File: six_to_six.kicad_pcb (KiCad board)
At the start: 2 copper layers, 545.4 x 309.1 mm, 468 parts, among them J1 Pads for coax, J10 Pads for coax, J11 Pads for coax, J12 Pads for coax, J13 BNC, J14 Pads for coax, J15 Pads for coax, J16 Pads for coax, J17 Pads for coax, J18 Relay control, J19 BNC, J2 Pads for coax, J20 Pads for coax, J21 Pads for coax, J22 Pads for coax, J23 BNC, J24 Pads for coax, J25 Pads for coax, J26 Pads for coax, J27 Pads for coax, J28 Relay control, J29 BNC, J3 BNC, J30 Pads for coax, J31 Pads for coax, J32 Pads for coax, J33 BNC, J34 Pads for coax, J35 Pads for coax, J36 Pads for coax, J37 Pads for coax, J38 Relay control, J39 BNC, J4 Pads for coax, J40 Pads for coax, J41 Pads for coax, J42 Pads for coax, J43 BNC, J44 Pads for coax, J45 Pads for coax, J46 Pads for coax, J47 Pads for coax, J48 Relay control, J49 BNC, J5 Pads for coax, J50 Pads for coax, J51 Pads for coax, J52 Pads for coax, J53 BNC, J54 Pads for coax, J55 Pads for coax, J56 Pads for coax, J57 Pads for coax, J58 Relay control, J59 BNC, J6 Pads for coax, J60 Pads for coax, J7 Pads for coax, J8 Relay control, J9 BNC, K1 RY-12W-K, K10 RY-12W-K, K11 RY-12W-K, K12 RY-12W-K, K13 RY-12W-K, K14 RY-12W-K, K15 RY-12W-K, K16 RY-12W-K, K17 RY-12W-K, K18 RY-12W-K, K19 RY-12W-K, K2 RY-12W-K, K20 RY-12W-K, K21 RY-12W-K, K22 RY-12W-K, K23 RY-12W-K, K24 RY-12W-K, K25 RY-12W-K, K26 RY-12W-K, K27 RY-12W-K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

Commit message: changed to 1 to 6
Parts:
- removed C12, C13, C17, C18, C19, C22, C23, C24, C28, C29, C30, C33, C34, C35, C39, C40, C41, C44, C45, C46, C50, C51, C52, C55, C56, C57, C61, C62, C63, C66: 100n, Capacitor_SMD:C_0603_1608Metric_Pad1.08x0.95mm_HandSolder
- removed C14, C25, C36, C47, C58: 100n, Capacitor_THT:C_Disc_D5.1mm_W3.2mm_P5.00mm
- removed C15, C16, C20, C21, C26, C27, C31, C32, C37, C38, C42, C43, C48, C49, C53, C54, C59, C60, C64, C65: 68p, Capacitor_THT:C_Disc_D5.1mm_W3.2mm_P5.00mm
- removed D11, D12, D17, D18, D19, D20, D21, D22, D27, D28, D29, D30, D31, D32, D37, D38, D39, D40, D41, D42, D47, D48, D49, D50, D51, D52, D57, D58, D59, D60: 1N4148W, Diode_SMD:D_SOD-123
- removed D13, D14, D15, D16, D23, D24, D25, D26, D33, D34, D35, D36, D43, D44, D45, D46, D53, D54, D55, D56: 1N4148, Diode_THT:D_DO-35_SOD27_P7.62mm_Horizontal
- removed F2, F3, F4, F5, F6: Polyfuse, Fuse:Fuse_BelFuse_0ZRE0005FF_L8.3mm_W3.8mm
- removed J10, J11, J12, J14, J15, J16, J20, J21, J22, J24, J25, J26, J30, J31, J32, J34, J35, J36, J40, J41, J42, J44, J45, J46, J50, J51, J52, J54, J55, J56, J60: Pads for coax, Connector_PinHeader_2.54mm:PinHeader_2x02_P2.54mm_Vertical
- removed J13, J19, J23, J29, J33, J39, J43, J49, J53, J59, J9: BNC, Components:BNC_vertical
- removed J17, J27, J37, J47, J57: Pads for coax, Connector_PinHeader_2.54mm:PinHeader_1x02_P2.54mm_Vertical
- removed J18, J28, J38, J48, J58: Relay control, Connector_PinHeader_2.54mm:PinHeader_2x04_P2.54mm_Vertical
- removed JP10, JP11, JP12, JP3, JP4, JP5, JP6, JP7, JP8, JP9: 50/75 ohm, Connector_PinHeader_2.54mm:PinHeader_1x03_P2.54mm_Vertical
- removed K10, K11, K12, K13, K14, K15, K16, K17, K18, K19, K20, K21, K22, K23, K24, K25, K26, K27, K28, K29, K30, K31, K32, K33, K34, K35, K36, K7, K8, K9: RY-12W-K, Components:RELAY_RY-12W-K
- removed NE2, NE3, NE4, NE5, NE6: Lamp_Neon, LED_THT:LED_D5.0mm_Clear
- removed Q10, Q11, Q12, Q13, Q14, Q15, Q16, Q17, Q18, Q19, Q20, Q21, Q22, Q23, Q24, Q25, Q26, Q27, Q28, Q29, Q30, Q31, Q32, Q33, Q34, Q35, Q36, Q7, Q8, Q9: MMBT3904, Package_TO_SOT_SMD:SOT-23
- removed R100, R101, R102, R24, R25, R26, R43, R44, R45, R62, R63, R64, R81, R82, R83: 68E, Resistor_THT:R_Axial_DIN0411_L9.9mm_D3.6mm_P12.70mm_Horizontal
- removed R103, R27, R46, R65, R84: 18E, Resistor_THT:R_Axial_DIN0411_L9.9mm_D3.6mm_P12.70mm_Horizontal
- removed R104, R111, R112, R28, R35, R36, R47, R54, R55, R66, R73, R74, R85, R92, R93: 100E, Resistor_THT:R_Axial_DIN0411_L9.9mm_D3.6mm_P12.70mm_Horizontal
- removed R105, R107, R109, R113, R20, R22, R29, R31, R33, R37, R39, R41, R48, R50, R52, R56, R58, R60, R67, R69, R71, R75, R77, R79, R86, R88, R90, R94, R96, R98: 3k3, Resistor_SMD:R_0603_1608Metric_Pad0.98x0.95mm_HandSolder
- removed R106, R108, R110, R114, R21, R23, R30, R32, R34, R38, R40, R42, R49, R51, R53, R57, R59, R61, R68, R70, R72, R76, R78, R80, R87, R89, R91, R95, R97, R99: 50E, Resistor_SMD:R_1210_3225Metric_Pad1.30x2.65mm_HandSolder
- removed TR13, TR25, TR37, TR49, TR61: BN-73-6802, Components:BN-73-6802-balun
- removed TR14, TR26, TR38, TR50, TR62: BN-73-transformer, Components:BN-73-202-1-1
- removed TR15, TR16, TR27, TR28, TR39, TR40, TR51, TR52, TR63, TR64: BN-73-202, Components:BN-73-202-2-0
- removed TR17, TR18, TR29, TR30, TR41, TR42, TR53, TR54, TR65, TR66: BN-73-6802, Components:BN-73-6802-2-0
- removed TR19, TR21, TR23, TR31, TR33, TR35, TR43, TR45, TR47, TR55, TR57, TR59, TR67, TR69, TR71: BN-73-6802, Components:BN-73-6802-3-0
- removed TR20, TR22, TR24, TR32, TR34, TR36, TR44, TR46, TR48, TR56, TR58, TR60, TR68, TR70, TR72: BN-73-6802, Components:BN-73-202-2-0
- C1, C2, C6, D1, D10, D2, D7, D8, D9, Q1, Q2, Q3, Q4, Q5, Q6, R10, R12, R2, R4: moved to B.Cu
- C10, C4, C5: value 68p -> 100n; footprint Capacitor_THT:C_Disc_D5.1mm_W3.2mm_P5.00mm -> Capacitor_SMD:C_0603_1608Metric_Pad1.08x0.95mm_HandSolder; moved to B.Cu
- C11, C7, C8: value 100n -> 68p; footprint Capacitor_SMD:C_0603_1608Metric_Pad1.08x0.95mm_HandSolder -> Capacitor_SMD:C_0805_2012Metric_Pad1.18x1.45mm_HandSolder; moved to B.Cu
- C3: footprint Capacitor_THT:C_Disc_D5.1mm_W3.2mm_P5.00mm -> Capacitor_SMD:C_0603_1608Metric_Pad1.08x0.95mm_HandSolder; moved to B.Cu
- C9: footprint Capacitor_THT:C_Disc_D5.1mm_W3.2mm_P5.00mm -> Capacitor_SMD:C_0805_2012Metric_Pad1.18x1.45mm_HandSolder; moved to B.Cu
- D3, D4, D5, D6: value 1N4148 -> 1N4148W; footprint Diode_THT:D_DO-35_SOD27_P7.62mm_Horizontal -> Diode_SMD:D_SOD-123; moved to B.Cu
- J1, J2, J4, J5, J6: value Pads for coax -> pads for coax; footprint Connector_PinHeader_2.54mm:PinHeader_2x02_P2.54mm_Vertical -> Components:Coax_pad
- J3: value BNC -> pads for coax; footprint Components:BNC_vertical -> Components:Coax_pad
- J7: value Pads for coax -> BNC; footprint Connector_PinHeader_2.54mm:PinHeader_1x02_P2.54mm_Vertical -> Components:BNC_vertical
- R1, R3: value 3k3 -> 50E; footprint Resistor_SMD:R_0603_1608Metric_Pad0.98x0.95mm_HandSolder -> Resistor_SMD:R_1210_3225Metric_Pad1.30x2.65mm_HandSolder; moved to B.Cu
- R11: value 50E -> 3k3; footprint Resistor_SMD:R_1210_3225Metric_Pad1.30x2.65mm_HandSolder -> Resistor_SMD:R_0603_1608Metric_Pad0.98x0.95mm_HandSolder; moved to B.Cu
- R13, R15: value 50E -> 100E; footprint Resistor_SMD:R_1210_3225Metric_Pad1.30x2.65mm_HandSolder -> Resistor_SMD:R_1206_3216Metric_Pad1.30x1.75mm_HandSolder; moved to B.Cu
- R14: value 3k3 -> 100E; footprint Resistor_SMD:R_0603_1608Metric_Pad0.98x0.95mm_HandSolder -> Resistor_SMD:R_1206_3216Metric_Pad1.30x1.75mm_HandSolder; moved to B.Cu
- R16, R17: value 100E -> 68E; footprint Resistor_THT:R_Axial_DIN0411_L9.9mm_D3.6mm_P12.70mm_Horizontal -> Resistor_SMD:R_1206_3216Metric_Pad1.30x1.75mm_HandSolder; moved to B.Cu
- R18: value 3k3 -> 68E; footprint Resistor_SMD:R_0603_1608Metric_Pad0.98x0.95mm_HandSolder -> Resistor_SMD:R_1206_3216Metric_Pad1.30x1.75mm_HandSolder; moved to B.Cu
- R19: value 50E -> 18E; footprint Resistor_SMD:R_1210_3225Metric_Pad1.30x2.65mm_HandSolder -> Resistor_SMD:R_1206_3216Metric_Pad1.30x1.75mm_HandSolder; moved to B.Cu
- R5, R6: value 68E -> 50E; footprint Resistor_THT:R_Axial_DIN0411_L9.9mm_D3.6mm_P12.70mm_Horizontal -> Resistor_SMD:R_1210_3225Metric_Pad1.30x2.65mm_HandSolder; moved to B.Cu
- R7: value 68E -> 3k3; footprint Resistor_THT:R_Axial_DIN0411_L9.9mm_D3.6mm_P12.70mm_Horizontal -> Resistor_SMD:R_0603_1608Metric_Pad0.98x0.95mm_HandSolder; moved to B.Cu
- R8: value 18E -> 3k3; footprint Resistor_THT:R_Axial_DIN0411_L9.9mm_D3.6mm_P12.70mm_Horizontal -> Resistor_SMD:R_0603_1608Metric_Pad0.98x0.95mm_HandSolder; moved to B.Cu
- R9: value 100E -> 3k3; footprint Resistor_THT:R_Axial_DIN0411_L9.9mm_D3.6mm_P12.70mm_Horizontal -> Resistor_SMD:R_0603_1608Metric_Pad0.98x0.95mm_HandSolder; moved to B.Cu
- TR1: footprint Components:BN-73-6802-balun -> Components:BN-73-6802-3-0
- TR10: footprint Components:BN-73-202-2-0 -> Components:BN-73-6802-2-0
- TR11: footprint Components:BN-73-6802-3-0 -> Components:BN-73-6802-balun
- TR12: value BN-73-6802 -> BN-73-transformer; footprint Components:BN-73-202-2-0 -> Components:BN-73-202-1-1
- TR2: value BN-73-transformer -> BN-73-6802; footprint Components:BN-73-202-1-1 -> Components:BN-73-202-2-0
- TR3: value BN-73-202 -> BN-73-6802; footprint Components:BN-73-202-2-0 -> Components:BN-73-6802-3-0
- TR4: value BN-73-202 -> BN-73-6802
- TR5: footprint Components:BN-73-6802-2-0 -> Components:BN-73-6802-3-0
- TR6: footprint Components:BN-73-6802-2-0 -> Components:BN-73-202-2-0
- TR7: value BN-73-6802 -> BN-73-202; footprint Components:BN-73-6802-3-0 -> Components:BN-73-202-2-0
- TR8: value BN-73-6802 -> BN-73-202
- TR9: footprint Components:BN-73-6802-3-0 -> Components:BN-73-6802-2-0
- moved C5 445.8 mm to (718.8, 217.2), turned to 180 degrees
- moved R9 441.8 mm to (722.6, 195.6), turned to 90 degrees
- moved TR8 408.5 mm to (622.3, 189.2)
- moved TR7 382.7 mm to (622.3, 207.0)
- moved Q3 326.4 mm to (718.8, 195.6), turned to 180 degrees
- moved K3 320.3 mm to (723.9, 195.6)
- moved D7 309.6 mm to (596.9, 180.3), turned to 180 degrees
- moved R11 307.5 mm to (722.6, 220.7), turned to 90 degrees
- moved J4 307.0 mm to (745.5, 211.1), turned to 180 degrees
- moved R10 296.0 mm to (722.6, 208.3), turned to 90 degrees
- moved C9 293.0 mm to (673.1, 228.6), turned to 180 degrees
- moved C6 292.4 mm to (718.8, 229.9), turned to 180 degrees
- moved TR9 288.8 mm to (613.4, 171.4)
- moved D9 267.6 mm to (603.6, 185.4), turned to 180 degrees
- moved TR10 265.1 mm to (613.4, 224.8)
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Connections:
- C1 pad 1: Net-(C1-Pad1) -> Net-(Q1-Pad1)
- C10 pad 2: GND -> Net-(C10-Pad2)
- C11 pad 1: Net-(C11-Pad1) -> Net-(TR7-Pad2)
- C2 pad 1: Net-(C2-Pad1) -> Net-(Q2-Pad1)
- C3 pad 1: Net-(C3-Pad1) -> Net-(Q3-Pad1)
- C3 pad 2: Net-(C3-Pad2) -> GND
- C4 pad 1: Net-(C4-Pad1) -> Net-(Q4-Pad1)
- C5 pad 1: Net-(C5-Pad1) -> Net-(Q5-Pad1)
- C6 pad 1: Net-(C6-Pad1) -> Net-(Q6-Pad1)
- C7 pad 1: Net-(C7-Pad1) -> Net-(TR1-Pad2)
- C8 pad 1: Net-(C8-Pad1) -> Net-(TR3-Pad2)
- C9 pad 1: Net-(C9-Pad1) -> Net-(TR5-Pad2)
- D10 pad 1: +12V -> Net-(D8-Pad2)
- D10 pad 2: Net-(D10-Pad2) -> Net-(D7-Pad1)
- D3 pad 1: Net-(D3-Pad1) -> +12V
- D3 pad 2: Net-(D3-Pad2) -> Net-(K3-Pad16)
- D4 pad 1: Net-(D3-Pad2) -> +12V
- D4 pad 2: GND -> Net-(K4-Pad16)
- D5 pad 1: Net-(D5-Pad1) -> +12V
- D5 pad 2: Net-(D3-Pad1) -> Net-(K5-Pad16)
- D6 pad 1: GND -> +12V
- D6 pad 2: Net-(D5-Pad1) -> Net-(K6-Pad16)
- D7 pad 1: +12V -> Net-(D7-Pad1)
- D7 pad 2: Net-(D7-Pad2) -> GND
- D8 pad 1: +12V -> Net-(D8-Pad1)
- D9 pad 1: +12V -> GND
- D9 pad 2: Net-(D9-Pad2) -> Net-(D8-Pad1)
- F1 pad 1: Net-(C3-Pad2) -> Net-(C10-Pad2)
- F1 pad 2: Net-(D3-Pad1) -> Net-(D8-Pad2)
- J1 pad 1: Net-(J1-Pad1) -> GND
- J1 pad 2: Net-(J1-Pad1) -> Net-(K1-Pad9)
- J2 pad 1: Net-(J2-Pad1) -> GND
- J2 pad 2: Net-(J2-Pad1) -> Net-(K2-Pad9)
- J3 pad 1: Net-(J3-Pad1) -> GND
- J3 pad 2: Net-(J3-Pad2) -> Net-(K3-Pad9)
- J4 pad 1: Net-(J4-Pad1) -> GND
- J4 pad 2: Net-(J4-Pad1) -> Net-(K4-Pad9)
- J5 pad 1: Net-(J5-Pad1) -> GND
- J5 pad 2: Net-(J5-Pad1) -> Net-(J5-Pad2)
- J6 pad 1: Net-(J6-Pad1) -> GND
- J6 pad 2: Net-(J6-Pad1) -> Net-(K6-Pad9)
- J7 pad 1: GND -> Net-(J7-Pad1)
- JP1 pad 2: Net-(D3-Pad1) -> Net-(D8-Pad2)
- K1 pad 13: /One to Six splitter/2-Way Splitter1/RF-out-2 -> /One to Six splitter/2-Way Splitter1/RF-out-1
- K1 pad 9: Net-(J1-Pad1) -> Net-(K1-Pad9)
- K2 pad 13: /One to Six splitter/2-Way Splitter3/RF-out-2 -> /One to Six splitter/2-Way Splitter1/RF-out-2
- K2 pad 9: Net-(J2-Pad1) -> Net-(K2-Pad9)
- K3 pad 13: /One to Six splitter/2-Way Splitter3/RF-out-1 -> /One to Six splitter/2-Way Splitter2/RF-out-1
- K3 pad 16: Net-(D7-Pad2) -> Net-(K3-Pad16)
- K3 pad 9: Net-(J4-Pad1) -> Net-(K3-Pad9)
- K4 pad 16: Net-(D8-Pad2) -> Net-(K4-Pad16)
- K4 pad 9: Net-(J5-Pad1) -> Net-(K4-Pad9)
- K5 pad 13: /One to Six splitter/2-Way Splitter2/RF-out-1 -> /One to Six splitter/2-Way Splitter3/RF-out-1
- K5 pad 16: Net-(D9-Pad2) -> Net-(K5-Pad16)
- K5 pad 9: Net-(J6-Pad1) -> Net-(J5-Pad2)
- K6 pad 13: /One to Six splitter/2-Way Splitter1/RF-out-1 -> /One to Six splitter/2-Way Splitter3/RF-out-2
- K6 pad 16: Net-(D10-Pad2) -> Net-(K6-Pad16)
- K6 pad 9: Net-(J10-Pad1) -> Net-(K6-Pad9)
- NE1 pad 1: Net-(J3-Pad2) -> Net-(J7-Pad2)
- NE1 pad 2: Net-(J3-Pad1) -> Net-(J7-Pad1)
- Q1 pad 1: Net-(C1-Pad1) -> Net-(Q1-Pad1)
- Q2 pad 1: Net-(C2-Pad1) -> Net-(Q2-Pad1)
- Q3 pad 1: Net-(C6-Pad1) -> Net-(Q3-Pad1)
- Q3 pad 3: Net-(D7-Pad2) -> Net-(K3-Pad16)
- Q4 pad 1: Net-(C7-Pad1) -> Net-(Q4-Pad1)
- Q4 pad 3: Net-(D8-Pad2) -> Net-(K4-Pad16)
- Q5 pad 1: Net-(C8-Pad1) -> Net-(Q5-Pad1)
- Q5 pad 3: Net-(D9-Pad2) -> Net-(K5-Pad16)
- Q6 pad 1: Net-(C11-Pad1) -> Net-(Q6-Pad1)
- Q6 pad 3: Net-(D10-Pad2) -> Net-(K6-Pad16)
- R1 pad 1: /One to Six splitter/Connectors/Relay-2 -> Net-(K1-Pad11)
- R1 pad 2: Net-(C1-Pad1) -> GND
- R10 pad 1: /One to Six splitter/Connectors/Relay-3 -> /One to Six splitter/Connectors/Relay-4
- R10 pad 2: Net-(C6-Pad1) -> Net-(Q4-Pad1)
- R11 pad 1: Net-(K3-Pad11) -> /One to Six splitter/Connectors/Relay-5
- R11 pad 2: GND -> Net-(Q5-Pad1)
- R12 pad 2: Net-(C7-Pad1) -> Net-(Q6-Pad1)
- R13 pad 1: Net-(K4-Pad11) -> /One to Six splitter/2-Way Splitter1/RF-out-1
- R13 pad 2: GND -> /One to Six splitter/2-Way Splitter1/RF-out-2
- R14 pad 1: /One to Six splitter/Connectors/Relay-5 -> /One to Six splitter/2-Way Splitter2/RF-out-1
- R14 pad 2: Net-(C8-Pad1) -> /One to Six splitter/2-Way Splitter2/RF-out-2
- R15 pad 1: Net-(K5-Pad11) -> /One to Six splitter/2-Way Splitter3/RF-out-1
- R15 pad 2: GND -> /One to Six splitter/2-Way Splitter3/RF-out-2
- R16 pad 1: /One to Six splitter/2-Way Splitter2/RF-out-1 -> Net-(TR8-Pad1)
- R16 pad 2: /One to Six splitter/2-Way Splitter2/RF-out-2 -> Net-(TR8-Pad4)
- R17 pad 1: /One to Six splitter/2-Way Splitter1/RF-out-1 -> /One to Six splitter/2-Way Splitter1/RF-in
- R17 pad 2: /One to Six splitter/2-Way Splitter1/RF-out-2 -> Net-(TR9-Pad4)
- R18 pad 1: /One to Six splitter/Connectors/Relay-1 -> Net-(TR9-Pad4)
- R18 pad 2: Net-(C11-Pad1) -> /One to Six splitter/2-Way Splitter3/RF-in
- R19 pad 1: Net-(K6-Pad11) -> /One to Six splitter/2-Way Splitter2/RF-in
- R19 pad 2: GND -> Net-(TR9-Pad4)
- R2 pad 1: Net-(K1-Pad11) -> Net-(K2-Pad11)
- R3 pad 1: /One to Six splitter/Connectors/Relay-4 -> Net-(K3-Pad11)
- R3 pad 2: Net-(C2-Pad1) -> GND
- R4 pad 1: Net-(K2-Pad11) -> Net-(K4-Pad11)
- R5 pad 1: Net-(R5-Pad1) -> Net-(K5-Pad11)
- R5 pad 2: Net-(R5-Pad2) -> GND
- R6 pad 1: /One to Six splitter/2-Way Splitter1/RF-in -> Net-(K6-Pad11)
- R6 pad 2: Net-(R6-Pad2) -> GND
- R7 pad 1: Net-(R6-Pad2) -> /One to Six splitter/Connectors/Relay-1
- R7 pad 2: /One to Six splitter/2-Way Splitter2/RF-in -> Net-(Q1-Pad1)
- R8 pad 1: /One to Six splitter/2-Way Splitter3/RF-in -> /One to Six splitter/Connectors/Relay-2
- R8 pad 2: Net-(R6-Pad2) -> Net-(Q2-Pad1)
- R9 pad 1: /One to Six splitter/2-Way Splitter3/RF-out-1 -> /One to Six splitter/Connectors/Relay-3
- R9 pad 2: /One to Six splitter/2-Way Splitter3/RF-out-2 -> Net-(Q3-Pad1)
- TR1 pad 1: Net-(J3-Pad1) -> /One to Six splitter/2-Way Splitter1/RF-in
- TR1 pad 2: Net-(C3-Pad1) -> Net-(TR1-Pad2)
- TR1 pad 3: Net-(J3-Pad2) -> Net-(TR1-Pad2)
- TR1 pad 4: GND -> Net-(TR1-Pad4)
- TR10 pad 1: /One to Six splitter/2-Way Splitter2/RF-out-1 -> Net-(TR9-Pad4)
- TR10 pad 2: Net-(C9-Pad1) -> Net-(TR8-Pad4)
- TR10 pad 3: Net-(C9-Pad1) -> Net-(TR8-Pad4)
- TR10 pad 4: /One to Six splitter/2-Way Splitter2/RF-out-2 -> /One to Six splitter/2-Way Splitter3/RF-in
- TR11 pad 1: /One to Six splitter/2-Way Splitter1/RF-in -> Net-(J7-Pad1)
- TR11 pad 3: Net-(C10-Pad1) -> Net-(J7-Pad2)
- TR11 pad 4: Net-(TR11-Pad4) -> GND
- TR12 pad 1: /One to Six splitter/2-Way Splitter1/RF-out-1 -> Net-(JP1-Pad1)
- TR12 pad 2: Net-(C10-Pad1) -> GND
- TR12 pad 3: Net-(C10-Pad1) -> Net-(JP2-Pad1)
- TR12 pad 4: /One to Six splitter/2-Way Splitter1/RF-out-2 -> GND
- TR2 pad 1: Net-(JP1-Pad1) -> /One to Six splitter/2-Way Splitter1/RF-out-1
- TR2 pad 2: GND -> Net-(TR1-Pad2)
- TR2 pad 3: Net-(JP2-Pad1) -> Net-(TR1-Pad2)
- TR2 pad 4: GND -> /One to Six splitter/2-Way Splitter1/RF-out-2
- TR3 pad 1: /One to Six splitter/3-Way Splitter/RF-in -> /One to Six splitter/2-Way Splitter2/RF-in
- TR3 pad 2: Net-(C4-Pad1) -> Net-(TR3-Pad2)
- TR3 pad 3: Net-(C4-Pad1) -> Net-(TR3-Pad2)
- TR3 pad 4: GND -> Net-(TR3-Pad4)
- TR4 pad 1: Net-(R5-Pad1) -> /One to Six splitter/2-Way Splitter2/RF-out-1
- TR4 pad 2: Net-(C4-Pad1) -> Net-(TR3-Pad2)
- TR4 pad 3: Net-(C4-Pad1) -> Net-(TR3-Pad2)
- TR4 pad 4: Net-(R5-Pad2) -> /One to Six splitter/2-Way Splitter2/RF-out-2
- TR5 pad 1: /One to Six splitter/2-Way Splitter1/RF-in -> /One to Six splitter/2-Way Splitter3/RF-in
- TR5 pad 2: Net-(R5-Pad1) -> Net-(TR5-Pad2)
- TR5 pad 3: Net-(R5-Pad1) -> Net-(TR5-Pad2)
- TR5 pad 4: Net-(R6-Pad2) -> Net-(TR5-Pad4)
- TR6 pad 1: Net-(R6-Pad2) -> /One to Six splitter/2-Way Splitter3/RF-out-1
- TR6 pad 2: Net-(R5-Pad2) -> Net-(TR5-Pad2)
- TR6 pad 3: Net-(R5-Pad2) -> Net-(TR5-Pad2)
- TR6 pad 4: /One to Six splitter/2-Way Splitter2/RF-in -> /One to Six splitter/2-Way Splitter3/RF-out-2
- TR7 pad 1: /One to Six splitter/2-Way Splitter3/RF-in -> /One to Six splitter/3-Way Splitter/RF-in
- TR7 pad 2: Net-(C5-Pad1) -> Net-(TR7-Pad2)
- TR7 pad 3: Net-(C5-Pad1) -> Net-(TR7-Pad2)
- TR7 pad 4: Net-(TR7-Pad4) -> GND
- TR8 pad 1: /One to Six splitter/2-Way Splitter3/RF-out-1 -> Net-(TR8-Pad1)
- TR8 pad 2: Net-(C5-Pad1) -> Net-(TR7-Pad2)
- TR8 pad 3: Net-(C5-Pad1) -> Net-(TR7-Pad2)
- TR8 pad 4: /One to Six splitter/2-Way Splitter3/RF-out-2 -> Net-(TR8-Pad4)
- TR9 pad 1: /One to Six splitter/2-Way Splitter2/RF-in -> /One to Six splitter/2-Way Splitter1/RF-in
- TR9 pad 2: Net-(C9-Pad1) -> Net-(TR8-Pad1)
- TR9 pad 3: Net-(C9-Pad1) -> Net-(TR8-Pad1)
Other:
- board size 545.4 x 309.1 mm -> 190.5 x 88.9 mm

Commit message: pcb routed and made gerbers
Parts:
- removed J4, J5, J6: pads for coax, Components:Coax_pad
- removed J8: Relay control, Connector_PinHeader_2.54mm:PinHeader_2x04_P2.54mm_Vertical
- removed JP1, JP2: 50/75 ohm, Connector_PinHeader_2.54mm:PinHeader_1x03_P2.54mm_Vertical
- removed TR12: BN-73-transformer, Components:BN-73-202-1-1
- added H1: M3, MountingHole:MountingHole_3.2mm_M3_DIN965_Pad, F.Cu at (646.4, 232.4)
- added H2: M3, MountingHole:MountingHole_3.2mm_M3_DIN965_Pad, F.Cu at (738.5, 232.4)
- added H3: M3, MountingHole:MountingHole_3.2mm_M3_DIN965_Pad, F.Cu at (738.5, 163.8)
- J1: value pads for coax -> RF Conn; footprint Components:Coax_pad -> Components:PinHeader_2x06_P2.54mm_Horizontal
- J2: value pads for coax -> limiter; footprint Components:Coax_pad -> Connector_PinHeader_2.54mm:PinHeader_1x02_P2.54mm_Vertical
- J3: value pads for coax -> Relay control; footprint Components:Coax_pad -> Connector_PinHeader_2.54mm:PinHeader_2x04_P2.54mm_Vertical
- J7: footprint Components:BNC_vertical -> Components:BNC_horizontal
- moved J2 102.7 mm to (645.4, 162.7), turned to 0 degrees
- moved C10 73.0 mm to (652.0, 163.4), turned to 90 degrees
- moved TR11 70.6 mm to (647.1, 202.2)
- moved J7 70.0 mm to (649.0, 219.1), turned to 90 degrees
- moved NE1 59.2 mm to (650.7, 208.0)
- moved F1 58.3 mm to (654.6, 164.3), turned to 180 degrees
- moved D10 55.6 mm to (651.8, 176.4), turned to -90 degrees
- moved TR10 54.9 mm to (659.1, 194.3)
- moved D7 54.9 mm to (651.8, 182.4), turned to -90 degrees
- moved TR9 46.4 mm to (659.1, 163.8)
- moved TR7 46.2 mm to (659.1, 179.1)
- moved R18 45.9 mm to (664.2, 198.1), turned to -90 degrees
- moved J3 44.3 mm to (719.5, 234.3), turned to 90 degrees
- moved D9 42.9 mm to (646.4, 182.4), turned to 90 degrees
- moved D8 42.1 mm to (646.4, 176.4), turned to 90 degrees
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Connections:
- D10 pad 1: Net-(D8-Pad2) -> Net-(D10-Pad1)
- D8 pad 2: Net-(D8-Pad2) -> Net-(D10-Pad1)
- F1 pad 2: Net-(D8-Pad2) -> /One to Six splitter/3-Way Splitter/RF-in
- J1 pad 1: GND -> /One to Six splitter/Connectors/RF-1
- J1 pad 2: Net-(K1-Pad9) -> GND
- J2 pad 1: GND -> /One to Six splitter/3-Way Splitter/RF-in
- J2 pad 2: Net-(K2-Pad9) -> Net-(D10-Pad1)
- J3 pad 2: Net-(K3-Pad9) -> +12V
- K1 pad 9: Net-(K1-Pad9) -> /One to Six splitter/Connectors/RF-1
- K2 pad 9: Net-(K2-Pad9) -> /One to Six splitter/Connectors/RF-2
- K3 pad 9: Net-(K3-Pad9) -> /One to Six splitter/Connectors/RF-3
- K4 pad 9: Net-(K4-Pad9) -> /One to Six splitter/Connectors/RF-4
- K5 pad 9: Net-(J5-Pad2) -> /One to Six splitter/Connectors/RF-5
- K6 pad 9: Net-(K6-Pad9) -> /One to Six splitter/Connectors/RF-6
- TR11 pad 1: Net-(J7-Pad1) -> Net-(J7-Pad2)
- TR11 pad 2: Net-(C10-Pad1) -> GND
- TR11 pad 3: Net-(J7-Pad2) -> Net-(J7-Pad1)
- TR11 pad 4: GND -> Net-(C10-Pad1)
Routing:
- net GND: track 0.00 -> 469.5 mm, vias 0 -> 12
- net /One to Six splitter/Connectors/Relay-1: track 0.00 -> 83.8 mm
- net +12V: track 0.00 -> 71.3 mm
- net /One to Six splitter/Connectors/Relay-2: track 0.00 -> 63.1 mm
- net Net-(R16-Pad1): track 0.00 -> 58.9 mm
- net Net-(C9-Pad1): track 0.00 -> 50.0 mm
- net Net-(R17-Pad2): track 0.00 -> 48.9 mm
- net /One to Six splitter/Connectors/Relay-3: track 0.00 -> 48.3 mm
- net Net-(C11-Pad1): track 0.00 -> 46.5 mm
- net /One to Six splitter/2-Way Splitter3/RF-out-1: track 0.00 -> 41.7 mm
- net /One to Six splitter/2-Way Splitter3/RF-out-2: track 0.00 -> 40.1 mm
- net /One to Six splitter/2-Way Splitter2/RF-out-1: track 0.00 -> 38.5 mm
- net /One to Six splitter/2-Way Splitter2/RF-out-2: track 0.00 -> 37.0 mm
- net /One to Six splitter/2-Way Splitter1/RF-out-2: track 0.00 -> 36.1 mm
- net /One to Six splitter/2-Way Splitter1/RF-out-1: track 0.00 -> 36.1 mm
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- added copper zone on B.Cu, net GND
- added copper zone on F.Cu, net GND
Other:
- board size 190.5 x 88.9 mm -> 99.8 x 77.5 mm

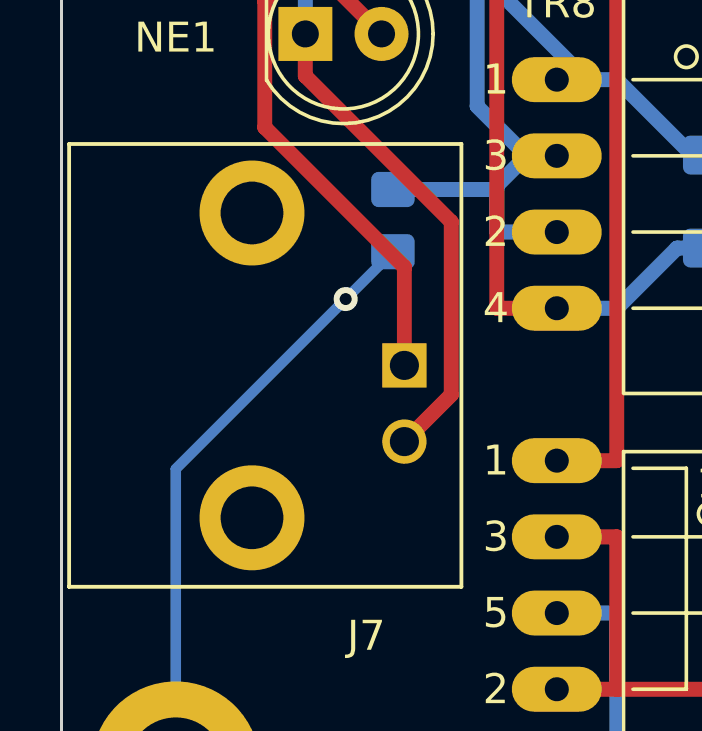
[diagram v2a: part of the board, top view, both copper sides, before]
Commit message: fixed BNC holes ans some silkscreen
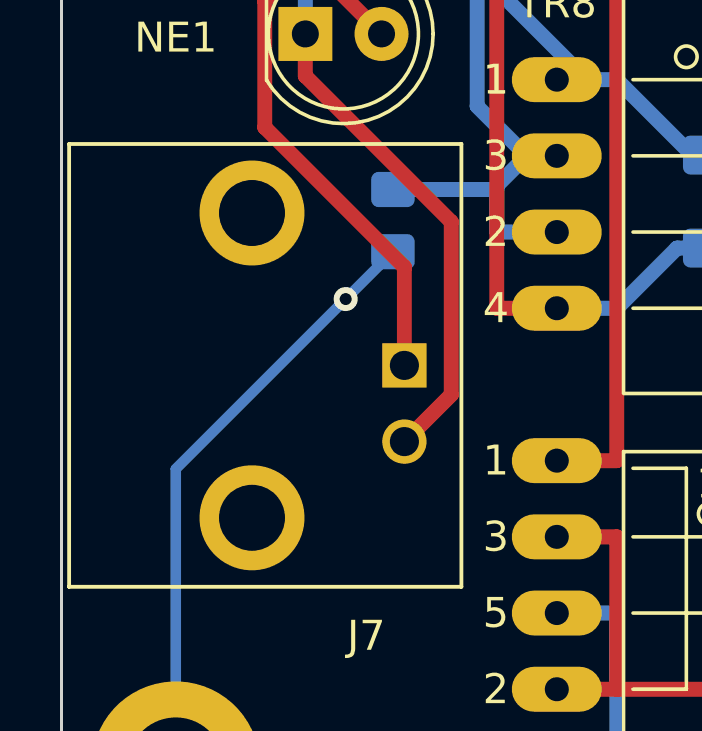
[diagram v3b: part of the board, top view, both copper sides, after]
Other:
- board text added: "six to six splitter/combiner rev: 1.0 12.03.2023 designed by: S59MZ"
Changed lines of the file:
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@@
       (effects (font (size 1 1) (thickness 0.15)))
     )
+    (fp_line (start 7.38 6.98) (end -7.38 6.98) (layer "F.SilkS") (width 0.127))
+    (fp_line (start -7.38 -6.096) (end 7.38 -6.096) (layer "F.SilkS") (width 0.127))
     (fp_line (start 7.38 -6.096) (end 7.38 6.98) (layer "F.SilkS") (width 0.127))
     (fp_line (start -7.38 6.98) (end -7.38 -6.096) (layer "F.SilkS") (width 0.127))
-    (fp_line (start 7.38 6.98) (end -7.38 6.98) (layer "F.SilkS") (width 0.127))
-    (fp_line (start -7.38 -6.096) (end 7.38 -6.096) (layer "F.SilkS") (width 0.127))
+    (fp_line (start -7.63 -28.83) (end 7.63 -28.83) (layer "F.CrtYd") (width 0.05))
     (fp_line (start 7.63 7.23) (end -7.63 7.23) (layer "F.CrtYd") (width 0.05))
     (fp_line (start -7.63 7.23) (end -7.63 -28.83) (layer "F.CrtYd") (width 0.05))
     (fp_line (start 7.63 -28.83) (end 7.63 7.23) (layer "F.CrtYd") (width 0.05))
-    (fp_line (start -7.63 -28.83) (end 7.63 -28.83) (layer "F.CrtYd") (width 0.05))
     (fp_line (start -7.38 6.98) (end -7.38 -28.58) (layer "F.Fab") (width 0.127))
-    (fp_line (start 7.38 6.98) (end -7.38 6.98) (layer "F.Fab") (width 0.127))
     (fp_line (start -7.38 -28.58) (end 7.38 -28.58) (layer "F.Fab") (width 0.127))
     (fp_line (start 7.38 -28.58) (end 7.38 6.98) (layer "F.Fab") (width 0.127))
-    (pad "" np_thru_hole circle locked (at -5.08 0 90) (size 3.5 3.5) (drill 2.09) (layers F&B.Cu *.Mask))
-    (pad "" np_thru_hole circle locked (at 5.08 0 90) (size 3.5 3.5) (drill 2.09) (layers F&B.Cu *.Mask))
+    (fp_line (start 7.38 6.98) (end -7.38 6.98) (layer "F.Fab") (width 0.127))
+    (pad "" thru_hole circle locked (at -5.08 0 90) (size 3.5 3.5) (drill 2.2) (layers *.Cu *.Mask))
+    (pad "" thru_hole circle locked (at 5.08 0 90) (size 3.5 3.5) (drill 2.2) (layers *.Cu *.Mask))
     (pad "1" thru_hole rect locked (at 0 5.08 90) (size 1.478 1.478) (drill 0.97) (layers *.Cu *.Mask)
       (net 70 "Net-(J7-Pad1)") (pinfunction "In") (pintype "passive"))
@@
   (gr_line (start 642.62 160.02) (end 642.62 236.22) (layer "Edge.Cuts") (width 0.1))
   (gr_line (start 742.442 160.02) (end 742.442 236.22) (layer "Edge.Cuts") (width 0.1))
+  (gr_text "six to six splitter/combiner\nrev: 1.0\n12.03.2023\ndesigned by: S59MZ" (at 697.738 215.265) (layer "B.SilkS")
+    (effects (font (size 1.2 1.2) (thickness 0.15)) (justify mirror))
+  )
   (segment (start 657.205 234.95) (end 654.665 232.41) (width 0.35) (layer "F.Cu") (net 1))
   (segment (start 654.665 232.41) (end 646.43 232.41) (width 0.35) (layer "F.Cu") (net 1))

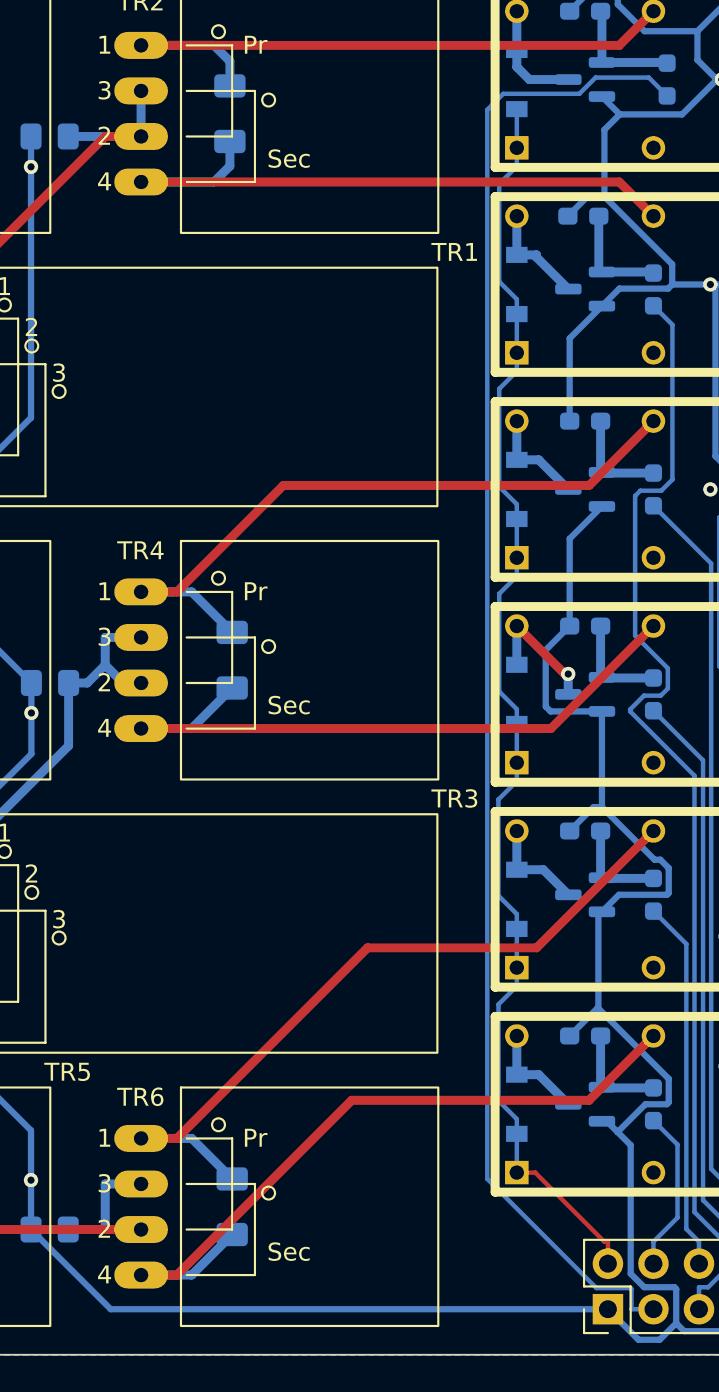
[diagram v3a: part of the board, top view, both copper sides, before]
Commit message: add block capacitor
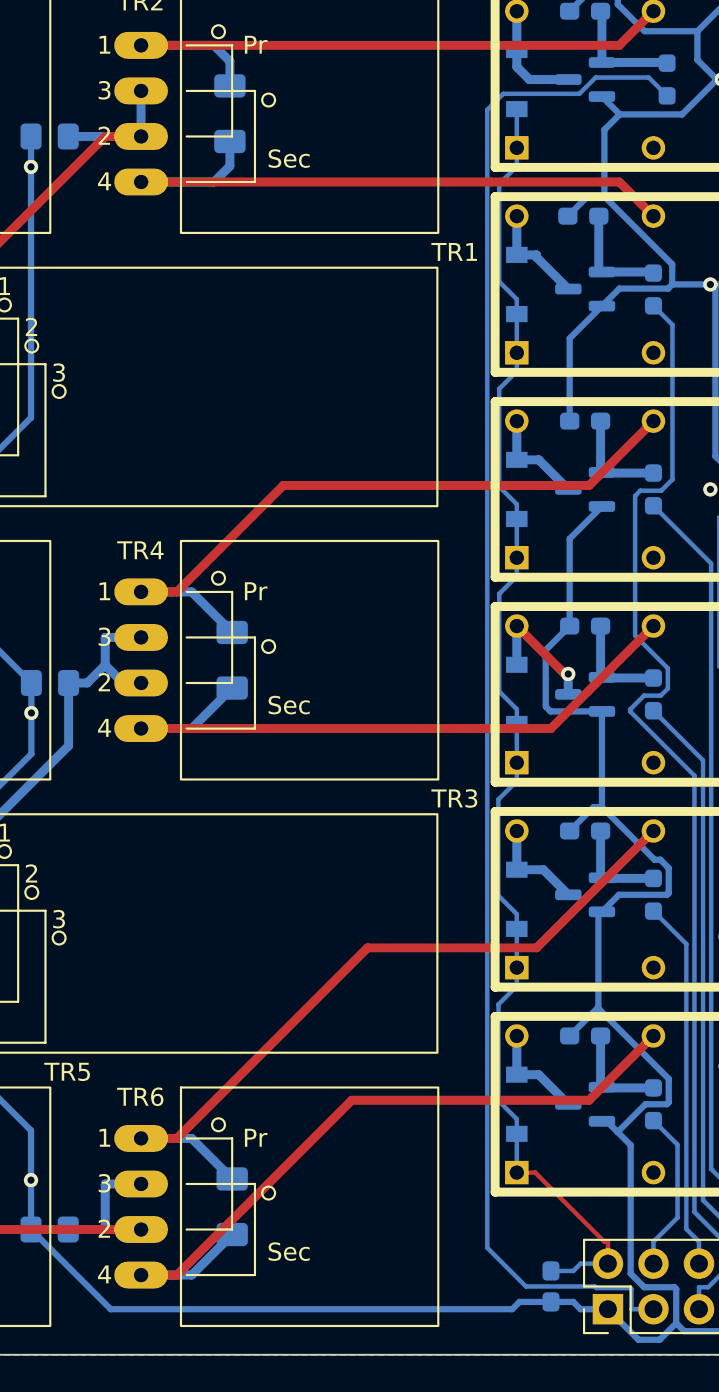
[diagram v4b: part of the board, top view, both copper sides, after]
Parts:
- added C12: 100n, Capacitor_SMD:C_0603_1608Metric_Pad1.08x0.95mm_HandSolder, B.Cu at (716.3, 233.0)
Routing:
- net +12V: track 71.3 -> 74.7 mm
- net /One to Six splitter/Connectors/Relay-1: track 83.8 -> 86.0 mm
